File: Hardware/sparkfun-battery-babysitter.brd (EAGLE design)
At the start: 33 x 33 mm, 55 parts, among them U1 BQ24075, U2 BQ27441-G1

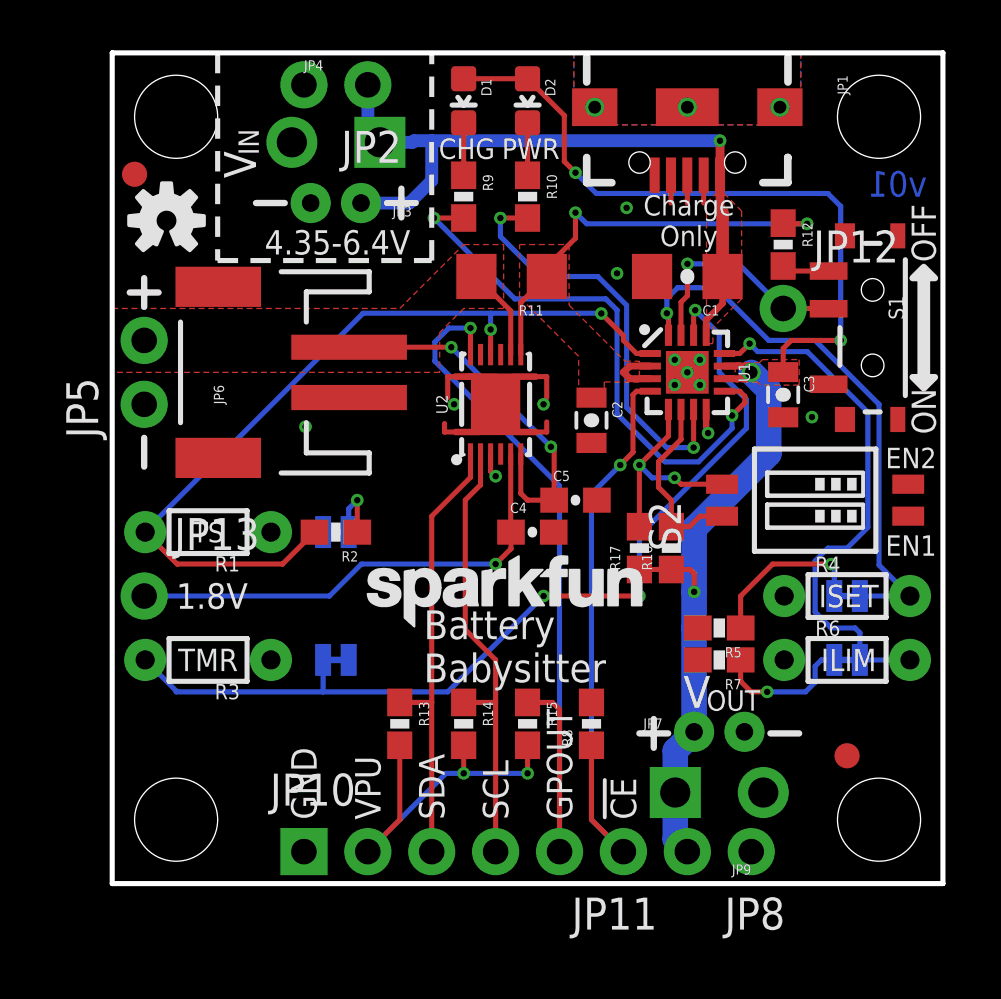
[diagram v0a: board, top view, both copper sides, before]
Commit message: Nudging sparkfun logo
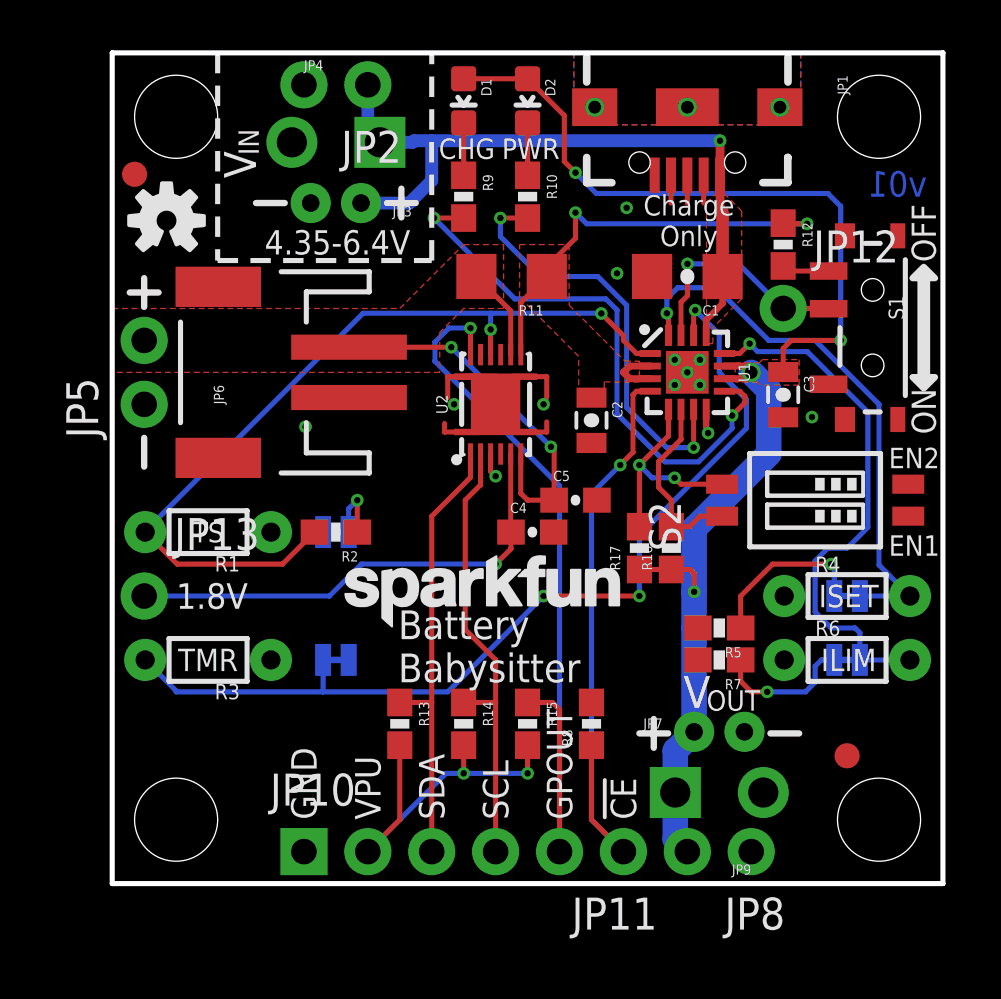
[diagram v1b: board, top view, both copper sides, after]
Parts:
- moved LOGO1 0.89 mm to (8.76, 9.72)
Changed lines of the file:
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@@
 <text x="15.24" y="2.54" size="1.016" layer="21" font="vector" ratio="15" rot="R90" align="center-left">SCL</text>
 <text x="10.16" y="2.54" size="1.016" layer="21" font="vector" ratio="15" rot="R90" align="center-left">VPU</text>
-<text x="12.3825" y="10.8585" size="1.143" layer="21" font="vector" ratio="15" align="top-left">Battery
+<text x="11.3665" y="10.8585" size="1.143" layer="21" font="vector" ratio="15" align="top-left">Battery
 Babysitter</text>
 <wire x1="10.922" y1="27.051" x2="12.065" y2="27.051" width="0.254" layer="21"/>
@@
 <text x="5.715" y="28.575" size="1.27" layer="21" font="vector" ratio="15" rot="R90" align="bottom-center">V</text>
 <text x="5.0165" y="28.956" size="0.8128" layer="21" font="vector" ratio="15" rot="R90" align="top-left">IN</text>
-<text x="31.75" y="13.843" size="0.8128" layer="21" font="vector" ratio="15" align="top-center">EN1</text>
-<text x="31.75" y="16.51" size="0.8128" layer="21" font="vector" ratio="15" align="bottom-center">EN2</text>
+<text x="31.877" y="13.843" size="0.8128" layer="21" font="vector" ratio="15" align="top-center">EN1</text>
+<text x="31.877" y="16.51" size="0.8128" layer="21" font="vector" ratio="15" align="bottom-center">EN2</text>
 </plain>
 <attributes>
@@
 <element name="SJ3" library="SparkFun-Passives" package="PAD-JUMPER-2-NC_BY_TRACE_YES_SILK" value="" x="29.21" y="11.43" rot="MR180"/>
 <element name="JP4" library="SparkFun-Connectors" package="JST-2-PTH-NS" value="" x="8.89" y="27.051"/>
-<element name="LOGO1" library="SparkFun-Aesthetics" package="SFE_LOGO_NAME_.1" value="SFE_LOGO_NAME.1_INCH" x="9.652" y="9.7155"/>
+<element name="LOGO1" library="SparkFun-Aesthetics" package="SFE_LOGO_NAME_.1" value="SFE_LOGO_NAME.1_INCH" x="8.763" y="9.7155"/>
 <element name="LOGO3" library="SparkFun-Aesthetics" package="OSHW-LOGO-S" value="OSHW-LOGOS" x="2.159" y="26.3525"/>
 <element name="R12" library="SparkFun-Resistors" package="0603-RES" value="100k" x="26.67" y="25.4" rot="R270">
@@
 <element name="FID2" library="SparkFun-Aesthetics" package="FIDUCIAL-1X2" value="FIDUCIAL1X2" x="29.21" y="5.08"/>
 <element name="S2" library="SparkFun-Electromechanical" package="DIPSWITCH-02-50MIL" value="" x="27.94" y="15.24" rot="R90">
-<attribute name="PROD_ID" value="TBD" x="27.94" y="15.24" size="1.778" layer="27" rot="R90" display="off"/>
+<attribute name="PROD_ID" value="SWCH-13215" x="27.94" y="15.24" size="1.778" layer="27" rot="R90" display="off"/>
 </element>
 </elements>

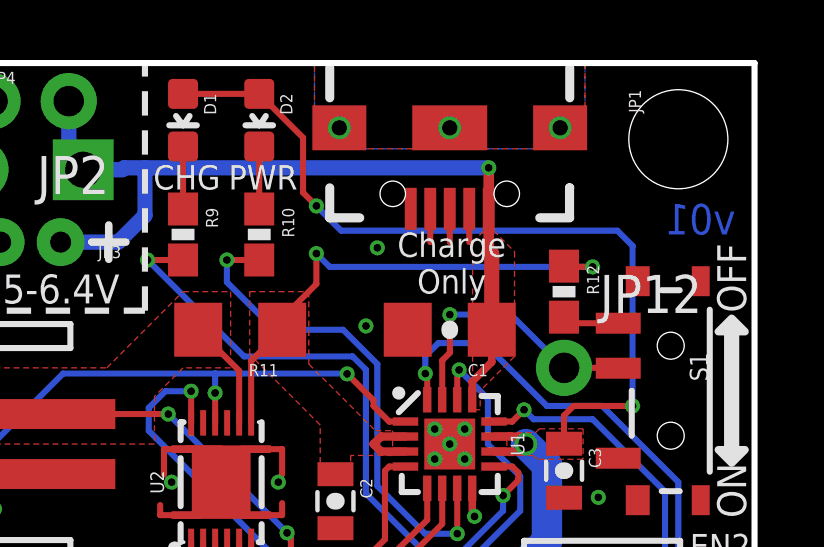
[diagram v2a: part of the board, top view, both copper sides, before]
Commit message: Adding SJ5, to set power LED to PWR or PGOOD.
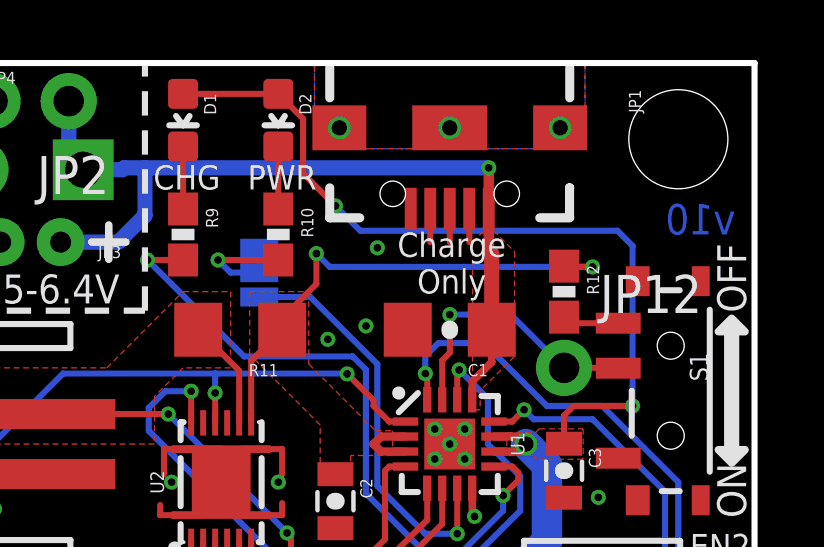
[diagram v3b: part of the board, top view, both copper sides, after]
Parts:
- added SJ5: (no value), SparkFun-Passives:PAD-JUMPER-3-2OF3_NC_BY_TRACE_YES_SILK_FULL_BOX
- R10: value 330 -> 1K
- moved D2 0.63 mm to (17.1, 31.1)
- moved R10 0.63 mm to (17.1, 27.3)
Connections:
- new net N$5: R10.2, SJ5.2
- net !PGOOD!: now also SJ5.1; no longer R10.2
- net GND: now also SJ5.3
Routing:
- net N$5: track 0.00 -> 3.55 mm, vias 0 -> 1
- net !PGOOD!: track 16.9 -> 13.8 mm, vias 2 -> 1
- net GND: vias 13 -> 14
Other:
- board text added: "!PGD!"
- board text added: "PWR-LED SEL"
- board text added: "v10"
- board text removed: "v01"
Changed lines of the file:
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@@
 <?xml version="1.0" encoding="utf-8"?>
 <!DOCTYPE eagle SYSTEM "eagle.dtd">
-<eagle version="7.1.0">
+<eagle version="7.5.0">
 <drawing>
 <settings>
@@
 <setting verticaltext="up"/>
 </settings>
-<grid distance="0.05" unitdist="inch" unit="inch" style="lines" multiple="1" display="yes" altdistance="0.005" altunitdist="inch" altunit="inch"/>
+<grid distance="0.025" unitdist="inch" unit="inch" style="lines" multiple="1" display="yes" altdistance="0.0025" altunitdist="inch" altunit="inch"/>
 <layers>
 <layer number="1" name="Top" color="4" fill="1" visible="yes" active="yes"/>
@@
 <wire x1="0" y1="0" x2="0" y2="33.02" width="0.2032" layer="20"/>
 <text x="14.097" y="29.21" size="0.8128" layer="21" font="vector" ratio="15" rot="R180" align="center">CHG</text>
-<text x="16.637" y="29.21" size="0.8128" layer="21" font="vector" ratio="15" align="center">PWR</text>
+<text x="17.272" y="29.21" size="0.8128" layer="21" font="vector" ratio="15" align="center">PWR</text>
 <text x="2.54" y="11.43" size="1.016" layer="21" font="vector" ratio="15" align="center-left">1.8V</text>
 <text x="17.78" y="2.54" size="1.016" layer="21" font="vector" ratio="15" rot="R90" align="center-left">GPOUT</text>
@@
 <text x="24.0665" y="14.1605" size="0.8128" layer="22" font="vector" ratio="15" rot="MR0" align="bottom-center">2</text>
 <text x="22.7965" y="14.1605" size="0.8128" layer="22" font="vector" ratio="15" rot="MR0" align="bottom-center">1</text>
-<text x="32.385" y="27.305" size="1.016" layer="16" ratio="15" rot="MR0">v01</text>
+<text x="32.385" y="27.305" size="1.016" layer="16" ratio="15" rot="MR0">v10</text>
 <text x="2.54" y="11.43" size="1.016" layer="22" font="vector" ratio="15" rot="MR180" align="center-left">1.8V</text>
 <text x="2.54" y="8.89" size="1.016" layer="22" font="vector" ratio="15" rot="MR180" align="center-left">TMR</text>
@@
 <text x="31.877" y="13.843" size="0.8128" layer="21" font="vector" ratio="15" align="top-center">EN1</text>
 <text x="31.877" y="16.51" size="0.8128" layer="21" font="vector" ratio="15" align="bottom-center">EN2</text>
+<text x="17.78" y="26.0985" size="0.8128" layer="22" font="vector" ratio="15" rot="MR90" align="bottom-center">PWR-LED
+SEL</text>
+<text x="16.4465" y="27.686" size="0.8128" layer="22" font="vector" ratio="15" rot="MR0" align="bottom-center">PWR</text>
+<text x="16.51" y="24.0665" size="0.8128" layer="22" font="vector" ratio="15" rot="MR0" align="top-center">!PGD!</text>
 </plain>
 <attributes>
@@
 <attribute name="VALUE" value="BLUE" x="13.97" y="31.115" size="1.778" layer="27" rot="R180" display="off"/>
 </element>
-<element name="D2" library="SparkFun-LED" package="LED-0603" value="RED" x="16.51" y="31.115" rot="R180">
-<attribute name="PROD_ID" value="DIO-00819" x="16.51" y="31.115" size="1.778" layer="27" rot="R180" display="off"/>
-<attribute name="VALUE" value="RED" x="16.51" y="31.115" size="1.778" layer="27" rot="R180" display="off"/>
+<element name="D2" library="SparkFun-LED" package="LED-0603" value="RED" x="17.145" y="31.115" rot="R180">
+<attribute name="PROD_ID" value="DIO-00819" x="17.145" y="31.115" size="1.778" layer="27" rot="R180" display="off"/>
+<attribute name="VALUE" value="RED" x="17.145" y="31.115" size="1.778" layer="27" rot="R180" display="off"/>
 </element>
 <element name="R9" library="SparkFun-Resistors" package="0603-RES" value="180" x="13.97" y="27.305" rot="R270">
@@
 <attribute name="VALUE" value="180" x="13.97" y="27.305" size="1.778" layer="27" rot="R270" display="off"/>
 </element>
-<element name="R10" library="SparkFun-Resistors" package="0603-RES" value="330" x="16.51" y="27.305" rot="R270">
-<attribute name="PROD_ID" value="RES-00818" x="16.51" y="27.305" size="1.778" layer="27" rot="R270" display="off"/>
-<attribute name="VALUE" value="330" x="16.51" y="27.305" size="1.778" layer="27" rot="R270" display="off"/>
+<element name="R10" library="SparkFun-Resistors" package="0603-RES" value="1K" x="17.145" y="27.305" rot="R270">
+<attribute name="PROD_ID" value="RES-07856" x="17.145" y="27.305" size="1.778" layer="27" rot="R270" display="off"/>
+<attribute name="VALUE" value="1K" x="17.145" y="27.305" size="1.778" layer="27" rot="R270" display="off"/>
 </element>
 <element name="C3" library="SparkFun-Capacitors" package="0805-CAP" value="10uF" x="26.67" y="19.431" rot="R270">
@@
 <attribute name="PROD_ID" value="SWCH-13215" x="27.94" y="15.24" size="1.778" layer="27" rot="R90" display="off"/>
 </element>
+<element name="SJ5" library="SparkFun-Passives" package="PAD-JUMPER-3-2OF3_NC_BY_TRACE_YES_SILK_FULL_BOX" value="" x="16.51" y="26.035" rot="MR90"/>
 </elements>
 <signals>
@@
 <contactref element="S2" pad="1"/>
 <contactref element="S2" pad="2"/>
+<contactref element="SJ5" pad="3"/>
+<via x="18.796" y="23.8125" extent="1-16" drill="0.254"/>
 </signal>
 <signal name="D+">
@@
 <contactref element="S1" pad="2"/>
 <via x="22.864" y="24.634" extent="1-16" drill="0.254"/>
-<wire x1="22.61" y1="21.795" x2="22.61" y2="23.11" width="0.2032" layer="1"/>
 <wire x1="22.864" y1="24.634" x2="24.896" y2="24.634" width="0.2032" layer="16"/>
 <wire x1="24.896" y1="24.634" x2="26.67" y2="22.86" width="0.2032" layer="16"/>
@@
 <wire x1="26.67" y1="22.86" x2="28.464" y2="22.86" width="0.2032" layer="1"/>
 <wire x1="28.464" y1="22.86" x2="28.476" y2="22.848" width="0.2032" layer="1"/>
+<wire x1="22.61" y1="21.795" x2="22.61" y2="23.11" width="0.2032" layer="1"/>
 </signal>
 <signal name="!CE!">
@@
 <contactref element="D2" pad="C"/>
 <contactref element="R10" pad="1"/>
-<wire x1="16.51" y1="28.155" x2="16.51" y2="30.238" width="0.2032" layer="1"/>
+<wire x1="17.145" y1="28.155" x2="17.145" y2="30.238" width="0.2032" layer="1"/>
 </signal>
 <signal name="!CHG!">
@@
 </signal>
 <signal name="!PGOOD!">
-<contactref element="U1" pad="7"/>
-<contactref element="R10" pad="2"/>
-<wire x1="23.11" y1="18.845" x2="23.11" y2="17.3315" width="0.2032" layer="1"/>
 <via x="23.11" y="17.3315" extent="1-16" drill="0.254"/>
 <wire x1="23.11" y1="17.3315" x2="22.0385" y2="17.3315" width="0.2032" layer="16"/>
 <wire x1="22.0385" y1="17.3315" x2="20.447" y2="18.923" width="0.2032" layer="16"/>
 <wire x1="20.447" y1="18.923" x2="20.447" y2="22.987" width="0.2032" layer="16"/>
-<wire x1="20.447" y1="22.987" x2="19.304" y2="24.13" width="0.2032" layer="16"/>
-<wire x1="19.304" y1="24.13" x2="17.018" y2="24.13" width="0.2032" layer="16"/>
-<via x="15.4305" y="26.455" extent="1-16" drill="0.254"/>
-<wire x1="17.018" y1="24.13" x2="15.4305" y2="25.7175" width="0.2032" layer="16"/>
-<wire x1="15.4305" y1="26.455" x2="15.4305" y2="25.7175" width="0.2032" layer="16"/>
-<wire x1="16.51" y1="26.455" x2="15.4305" y2="26.455" width="0.2032" layer="1"/>
+<wire x1="20.447" y1="22.987" x2="18.2118" y2="25.2222" width="0.2032" layer="16"/>
+<contactref element="U1" pad="7"/>
+<contactref element="SJ5" pad="1"/>
+<wire x1="16.51" y1="25.2222" x2="18.2118" y2="25.2222" width="0.2032" layer="16"/>
+<wire x1="23.11" y1="18.845" x2="23.11" y2="17.3315" width="0.2032" layer="1"/>
 </signal>
 <signal name="N$4">
@@
 <wire x1="22.38" y1="5.2825" x2="22.38" y2="3.6195" width="1.016" layer="16"/>
 <wire x1="22.38" y1="1.75" x2="22.38" y2="3.6195" width="1.016" layer="16"/>
-<via x="18.415" y="28.2575" extent="1-16" drill="0.254"/>
-<wire x1="18.415" y1="28.2575" x2="17.9705" y2="28.702" width="0.2032" layer="1"/>
-<wire x1="17.9705" y1="28.702" x2="17.9705" y2="30.5315" width="0.2032" layer="1"/>
-<wire x1="18.415" y1="28.2575" x2="19.2405" y2="27.432" width="0.2032" layer="16"/>
-<wire x1="19.2405" y1="27.432" x2="28.448" y2="27.432" width="0.2032" layer="16"/>
+<via x="19.05" y="28.2575" extent="1-16" drill="0.254"/>
+<wire x1="19.05" y1="28.2575" x2="17.9705" y2="29.337" width="0.2032" layer="1"/>
+<wire x1="17.9705" y1="29.337" x2="17.9705" y2="31.1665" width="0.2032" layer="1"/>
+<wire x1="19.05" y1="28.2575" x2="19.8755" y2="27.432" width="0.2032" layer="16"/>
+<wire x1="19.8755" y1="27.432" x2="28.448" y2="27.432" width="0.2032" layer="16"/>
 <wire x1="28.956" y1="21.59" x2="28.956" y2="26.924" width="0.2032" layer="16"/>
 <wire x1="28.956" y1="26.924" x2="28.448" y2="27.432" width="0.2032" layer="16"/>
 <wire x1="26.0985" y1="17.0815" x2="26.0985" y2="19.6215" width="1.016" layer="16"/>
 <wire x1="26.0985" y1="19.6215" x2="25.4" y2="20.32" width="1.016" layer="16"/>
-<wire x1="16.51" y1="31.992" x2="17.9705" y2="30.5315" width="0.2032" layer="1"/>
-<wire x1="13.97" y1="31.992" x2="16.51" y2="31.992" width="0.2032" layer="1"/>
+<wire x1="17.145" y1="31.992" x2="17.9705" y2="31.1665" width="0.2032" layer="1"/>
+<wire x1="13.97" y1="31.992" x2="17.145" y2="31.992" width="0.2032" layer="1"/>
 <via x="23.13" y="11.596" extent="1-16" drill="0.254"/>
 <wire x1="23.13" y1="11.596" x2="23.13" y2="14.113" width="1.016" layer="16"/>
@@
 <wire x1="22.21" y1="28.161" x2="22.21" y2="27.051" width="0.2032" layer="1"/>
 </signal>
+<signal name="N$5">
+<contactref element="R10" pad="2"/>
+<contactref element="SJ5" pad="2"/>
+<wire x1="17.145" y1="26.455" x2="15.1375" y2="26.455" width="0.2032" layer="1"/>
+<via x="15.1375" y="26.455" extent="1-16" drill="0.254"/>
+<wire x1="15.1375" y1="26.455" x2="15.5575" y2="26.035" width="0.2032" layer="16"/>
+<wire x1="15.5575" y1="26.035" x2="16.51" y2="26.035" width="0.2032" layer="16"/>
+</signal>
 </signals>
